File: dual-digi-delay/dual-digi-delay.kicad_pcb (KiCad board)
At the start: 2 copper layers, 148.8 x 152.9 mm, 214 parts, among them J1 TopBoardPowerRecv, J10 Delay Time Control, J11 Delay1_CV, J12 Delay1_CV, J13 Delay Send, J14 LowerBoardPowerSend, J15 Main Power, J16 Feedback Audio, J2 DelayAudio, J20 MidBoardPowerSend, J21 Delay Time Control, J23 Delay Out, J24 Output Audio, J25 DELAY2_CV, J26 DELAY1_CV, J27 AUDIO_IN, J28 MIX_OUT, J29 DELAY1_WET_OUT, J3 Input Audio, J30 DELAY2_WET_OUT, J31 Feedback Audio, J32 Delay Send, J33 Delay Return, J38 Delay2_CV, J39 Delay2_CV, J4 Output Audio, J5 Delay Out, J6 DelayAudio, J7 Input Audio, J8 Delay Return, J9 MidBoardPowerRecv, Q1 2N3904, Q2 2N3904, Q3 2N3904, Q4 2N3904, Q5 2N3904, Q6 2N3904, SW1 CV_JOIN, SW2 Delay 2 Input, U1 TL072, U2 TL072, U3 PT2399, U4 PT2399, U5 TL074, U6 TL074, U7 LM7805_TO220, U8 TL072

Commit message: Finalising rev 01 of dual digi delay
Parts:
- added G***: LOGO, rumblesan-footprints:Logo_Ammonite-simple_10.4mmx12.0mm, B.Cu at (145.8, 34.8)
- R37, R43: value 100k -> 220k
- R42: value 47k -> 100k
- moved R44 28.6 mm to (110.5, 107.7)
- moved R39 27.5 mm to (92.2, 134.6)
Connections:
- net /Power/+V renamed +12V
- net /Power/-V renamed -12V
- H1 pad 1: /TOP_0V -> GND
- H2 pad 1: /TOP_0V -> GND
- H3 pad 1: /MID_0V -> GND
- H4 pad 1: /MID_0V -> GND
- R39 pad 2: /MID_+V -> /MID_-V
- R44 pad 2: /MID_+V -> /MID_-V
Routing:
- net Net-(C44-Pad2): track 41.7 -> 29.4 mm
- net Net-(C43-Pad2): track 30.0 -> 42.1 mm
- net /MID_-V: track 179.7 -> 186.0 mm
- net /MID_+V: track 155.6 -> 149.7 mm
- net Net-(C41-Pad1): track 28.6 -> 30.2 mm
- net /CVControl/DELAY1_CV_JOIN_OUT: track 38.9 -> 39.7 mm
- net /MID_0V: vias 20 -> 26

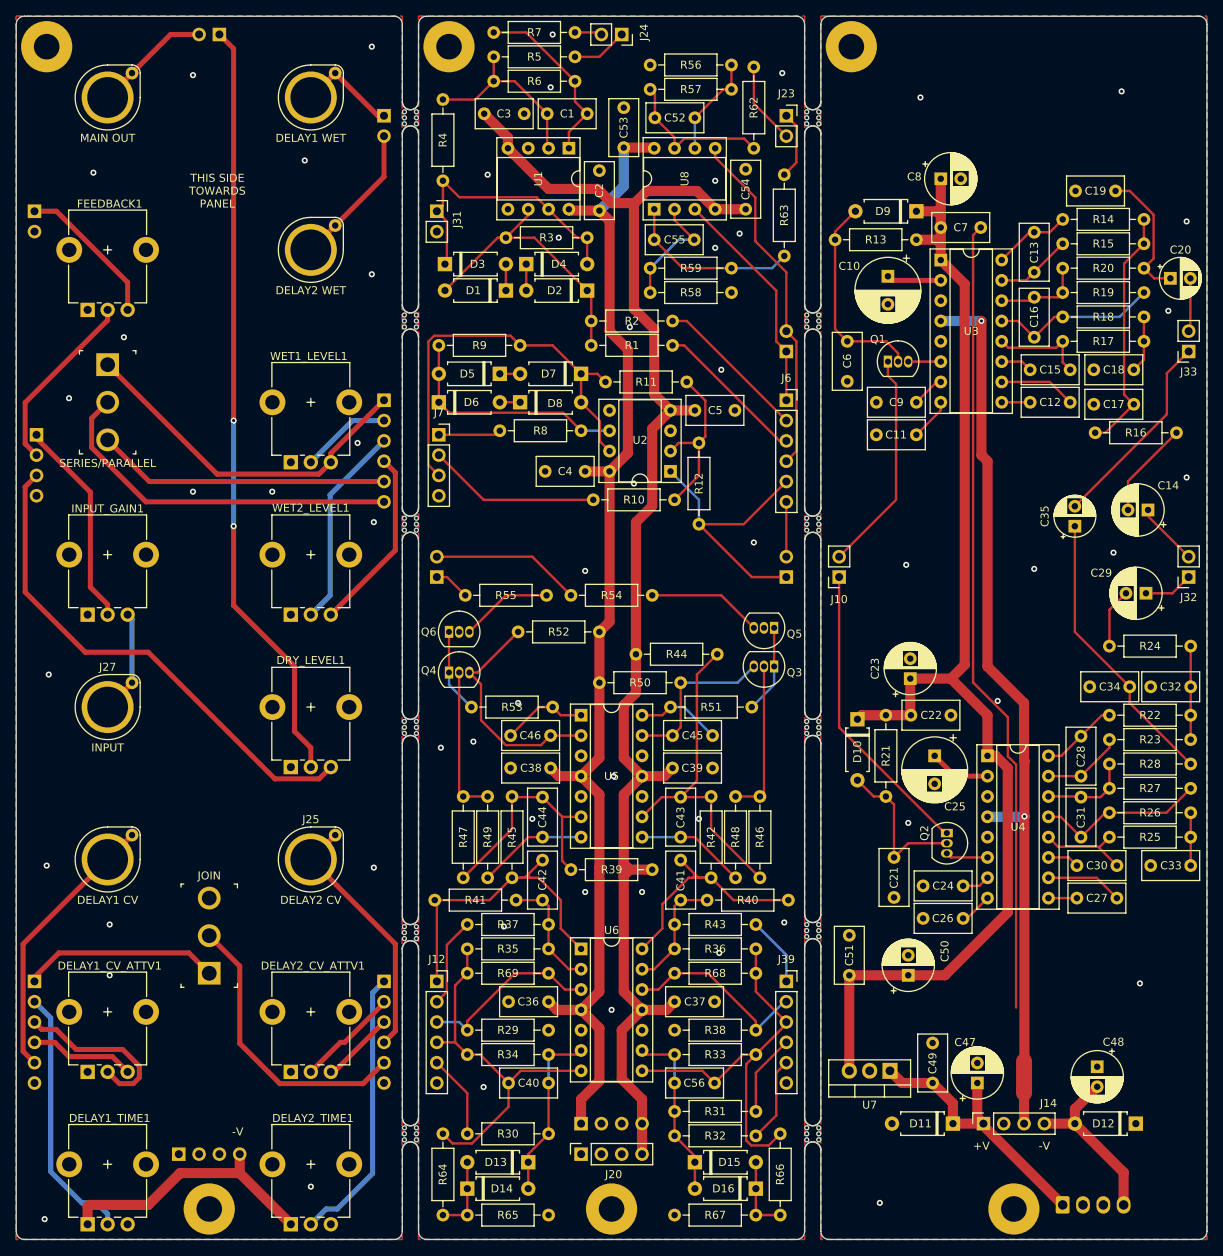
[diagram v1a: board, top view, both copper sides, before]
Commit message: Updating digi delay to rev 2
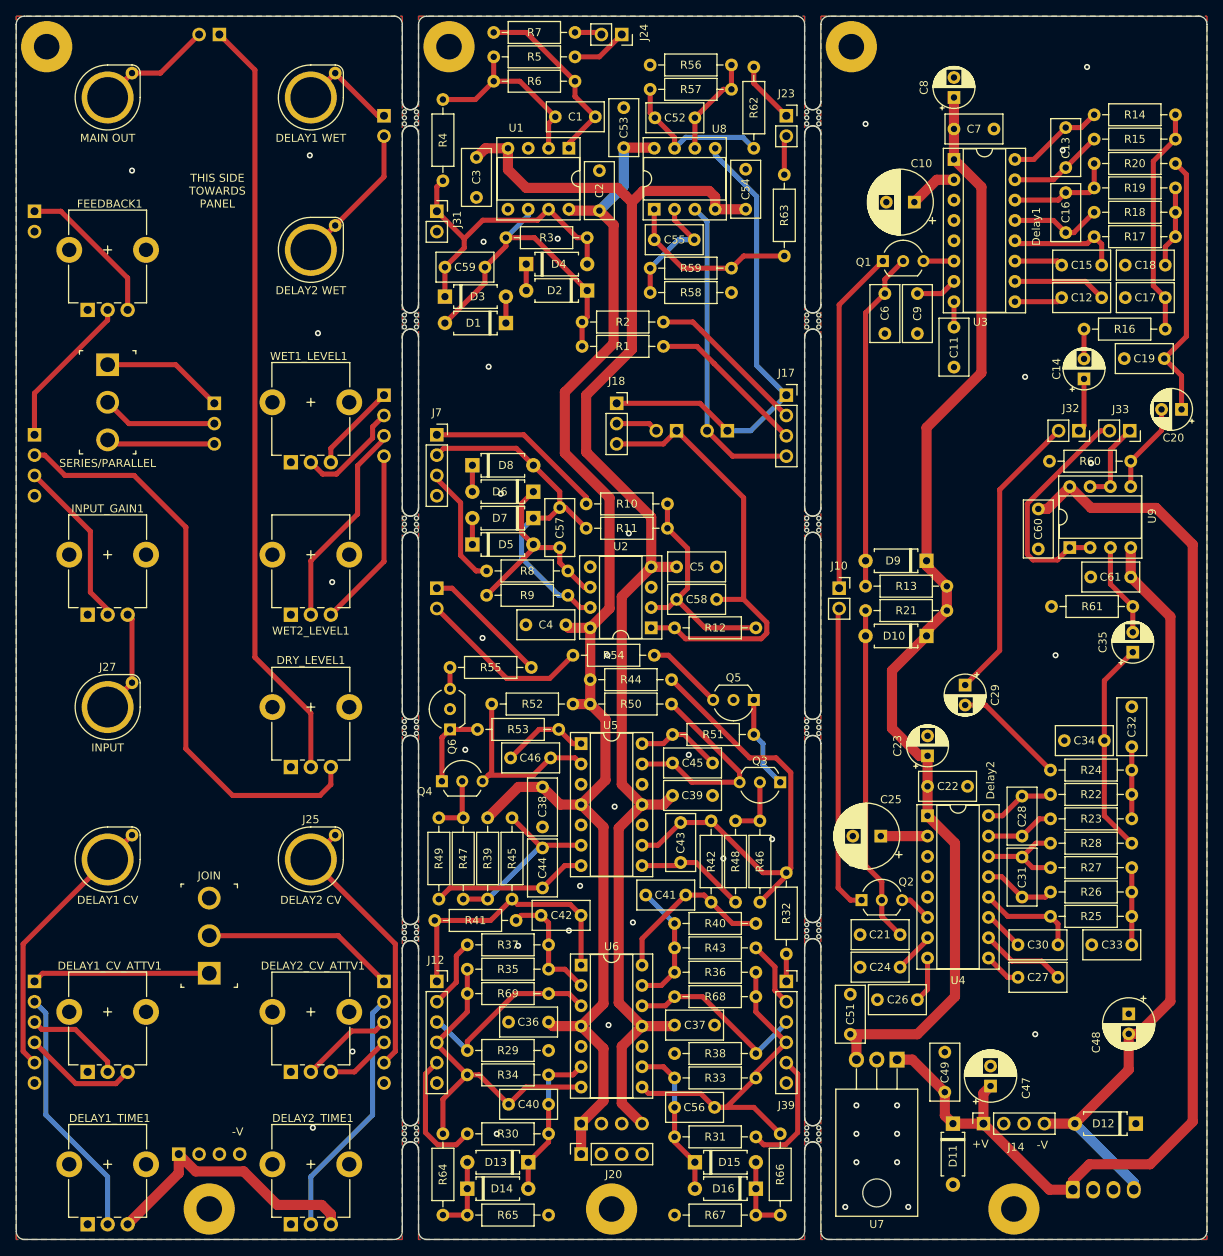
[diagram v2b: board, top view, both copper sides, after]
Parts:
- removed C50: 10uF, rumblesan-footprints:CP_Radial_D6.3mm_P2.50mm
- removed G***: LOGO, rumblesan-footprints:Logo_Ammonite-simple_10.4mmx12.0mm
- removed NT1: Net-Tie_2, NetTie:NetTie-2_SMD_Pad2.0mm
- removed mouse-bite-2mm-slot (x12): VAL**, Panelization:mouse-bite-2mm-slot
- added C57: 10pF, rumblesan-footprints:C_Rect_L7.0mm_W3.5mm_P5.00mm, F.Cu at (90.8, 89.4)
- added C58: 10pF, rumblesan-footprints:C_Rect_L7.0mm_W3.5mm_P5.00mm, F.Cu at (110.4, 100.8)
- added C59: 10pF, rumblesan-footprints:C_Rect_L7.0mm_W3.5mm_P5.00mm, F.Cu at (76.5, 59.3)
- added C60: 100nF, rumblesan-footprints:C_Rect_L7.0mm_W3.5mm_P5.00mm, F.Cu at (150.6, 94.5)
- added C61: 100nF, rumblesan-footprints:C_Rect_L7.0mm_W3.5mm_P5.00mm, F.Cu at (162.2, 98.0)
- added H10: MouseBite, Panelization:mouse-bite-2mm-slot, F.Cu at (72.1, 142.5)
- added H11: MouseBite, Panelization:mouse-bite-2mm-slot, F.Cu at (72.1, 91.4)
- added H12: MouseBite, Panelization:mouse-bite-2mm-slot, F.Cu at (122.4, 40.6)
- added H13: MouseBite, Panelization:mouse-bite-2mm-slot, F.Cu at (72.1, 40.6)
- added H14: MouseBite, Panelization:mouse-bite-2mm-slot, F.Cu at (72.1, 116.8)
- added H15: MouseBite, Panelization:mouse-bite-2mm-slot, F.Cu at (122.4, 167.6)
- added H16: MouseBite, Panelization:mouse-bite-2mm-slot, F.Cu at (122.4, 66.0)
- added H17: MouseBite, Panelization:mouse-bite-2mm-slot, F.Cu at (72.1, 66.0)
- added H18: MouseBite, Panelization:mouse-bite-2mm-slot, F.Cu at (122.4, 142.2)
- added H19: Logo_Ammonite-simple, rumblesan-footprints:Logo_Ammonite-simple_10.4mmx12.0mm, B.Cu at (134.1, 82.7)
- added H7: MouseBite, Panelization:mouse-bite-2mm-slot, F.Cu at (72.1, 167.6)
- added H8: MouseBite, Panelization:mouse-bite-2mm-slot, F.Cu at (122.4, 91.4)
- added H9: MouseBite, Panelization:mouse-bite-2mm-slot, F.Cu at (122.4, 116.8)
- added J17: Delay Audio, Connector_PinSocket_2.54mm:PinSocket_1x04_P2.54mm_Vertical, F.Cu at (119.1, 75.3)
- added J18: Delay2 Source, Connector_PinSocket_2.54mm:PinSocket_1x03_P2.54mm_Vertical, F.Cu at (97.9, 76.3)
- added R60: 100k, rumblesan-footprints:Resistor_THT_L6.3mm_D2.5mm_P10.16mm_Horizontal, F.Cu at (162.2, 83.6)
- added R61: 100k, rumblesan-footprints:Resistor_THT_L6.3mm_D2.5mm_P10.16mm_Horizontal, F.Cu at (162.4, 101.7)
- added U9: TL072, rumblesan-footprints:DIP-8_W7.62mm_Socket, F.Cu at (154.6, 94.4)
- C13, C28: value 100nF -> 560pF
- C14, C29: value 4.7uF -> 10uF; footprint rumblesan-footprints:CP_Radial_D6.3mm_P2.50mm -> rumblesan-footprints:CP_Radial_D5.0mm_P2.50mm
- C20, C35: value 1uF -> 10uF
- C23, C8: footprint rumblesan-footprints:CP_Radial_D6.3mm_P2.50mm -> rumblesan-footprints:CP_Radial_D5.0mm_P2.50mm
- J2: value DelayAudio -> Delay Audio; footprint Connector_PinHeader_2.54mm:PinHeader_1x06_P2.54mm_Vertical -> Connector_PinHeader_2.54mm:PinHeader_1x04_P2.54mm_Vertical
- J25: value DELAY2_CV -> BananaJack_PanelMount
- J26: value DELAY1_CV -> BananaJack_PanelMount
- J27: value AUDIO_IN -> BananaJack_PanelMount
- J28: value MIX_OUT -> BananaJack_PanelMount
- J29: value DELAY1_WET_OUT -> BananaJack_PanelMount
- J30: value DELAY2_WET_OUT -> BananaJack_PanelMount
- J6: value DelayAudio -> Delay2 Source; footprint Connector_PinSocket_2.54mm:PinSocket_1x06_P2.54mm_Vertical -> Connector_PinHeader_2.54mm:PinHeader_1x03_P2.54mm_Vertical; moved to B.Cu
- Q1, Q2, Q3, Q4, Q5, Q6: footprint Package_TO_SOT_THT:TO-92_Inline -> Package_TO_SOT_THT:TO-92_Inline_Wide
- R1, R2: value 100k -> 47k
- R13, R21: value 220k -> 560k
- R32, R42, R45: value 100k -> 56k
- R39, R44: value 220k -> 150k
- R4, R5, R56, R58: value 27k -> 15k
- R57, R59: value 82k -> 100k
- R9: value 27k -> 33k
- SW1: value CV_JOIN -> SW_SPST
- SW2: value Delay 2 Input -> SW_SPDT
- U7: footprint Package_TO_SOT_THT:TO-220-3_Vertical -> Package_TO_SOT_THT:TO-220-3_Horizontal_TabDown
- moved J6 71.5 mm to (47.6, 76.3), turned to 180 degrees
- moved D9 43.7 mm to (136.7, 96.0)
- moved R13 43.5 mm to (139.2, 99.2)
- moved R9 31.8 mm to (91.8, 100.3)
- moved C29 25.3 mm to (141.5, 111.5), turned to 270 degrees
- moved R32 23.1 mm to (119.1, 145.2), turned to 90 degrees
- moved J13 22.9 mm to (105.4, 79.8), turned to 90 degrees
- moved J32 22.9 mm to (155.7, 79.8), turned to 270 degrees
- moved C19 21.8 mm to (161.4, 70.7)
- moved D5 21.6 mm to (79.9, 94.0), turned to 0 degrees
- moved U2 19.7 mm to (102.2, 104.4)
- moved C5 19.7 mm to (105.4, 96.8)
- moved C4 19.3 mm to (86.6, 104.0)
- moved D7 19.0 mm to (87.5, 90.7)
- moved R11 18.4 mm to (104.3, 91.9)
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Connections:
- C14 pad 1: /PT2399-Delay-2/AUDIO_IN -> /PT2399-Delay-1/AUDIO_IN
- C2 pad 1: /MID_0V -> GND
- C2 pad 2: /MID_+V -> +12V
- C20 pad 2: /PT2399-Delay-2/AUDIO_OUT -> /PT2399-Delay-1/AUDIO_OUT
- C29 pad 1: /PT2399-Delay-1/AUDIO_IN -> /PT2399-Delay-2/AUDIO_IN
- C3 pad 1: /MID_-V -> -12V
- C3 pad 2: /MID_0V -> GND
- C35 pad 2: /PT2399-Delay-1/AUDIO_OUT -> /PT2399-Delay-2/AUDIO_OUT
- C36 pad 1: /MID_0V -> GND
- C36 pad 2: /MID_+V -> +12V
- C37 pad 1: /MID_-V -> -12V
- C37 pad 2: /MID_0V -> GND
- C38 pad 1: /MID_0V -> GND
- C38 pad 2: /MID_+V -> +12V
- C39 pad 1: /MID_-V -> -12V
- C39 pad 2: /MID_0V -> GND
- C4 pad 1: /MID_0V -> GND
- C4 pad 2: /MID_+V -> +12V
- C5 pad 1: /MID_-V -> -12V
- C5 pad 2: /MID_0V -> GND
- C53 pad 1: /MID_0V -> GND
- C53 pad 2: /MID_+V -> +12V
- C54 pad 1: /MID_-V -> -12V
- C54 pad 2: /MID_0V -> GND
- DELAY1_CV_ATTV1 pad 1: /TOP_0V -> GND
- DELAY1_TIME1 pad 1: /CVInputs/-V -> GND
- DELAY1_TIME1 pad 3: /TOP_0V -> +12V
- DELAY2_CV_ATTV1 pad 1: /TOP_0V -> GND
- DELAY2_TIME1 pad 1: /CVInputs/-V -> GND
- DELAY2_TIME1 pad 3: /TOP_0V -> +12V
- DRY_LEVEL1 pad 1: /TOP_0V -> GND
- FEEDBACK1 pad 1: /TOP_0V -> GND
- INPUT_GAIN1 pad 1: /TOP_0V -> GND
- J1 pad 1: /TOP_0V -> +12V
- J1 pad 2: /TOP_0V -> GND
- J1 pad 3: /TOP_0V -> GND
- J1 pad 4: /CVInputs/-V -> GND
- J11 pad 6: /TOP_0V -> GND
- J12 pad 6: /MID_0V -> GND
- J16 pad 2: /TOP_0V -> GND
- J20 pad 1: /MID_0V -> +12V
- J20 pad 2: /MID_0V -> GND
- J20 pad 3: /MID_0V -> GND
- J20 pad 4: /MID_-V -> GND
- J3 pad 1: /AudioIO/AUDIO_IN -> /AudioIO/FEEDBACK_LEVEL
- J3 pad 2: /AudioIO/FEEDBACK_LEVEL -> /AudioIO/DRY_AUDIO_INPUT
- J3 pad 3: /AudioIO/DRY_AUDIO_INPUT -> /AudioIO/AUDIO_IN
- J3 pad 4: /TOP_0V -> GND
- J31 pad 2: /MID_0V -> GND
- J33 pad 1: /PT2399-Delay-1/AUDIO_OUT -> /DelayBuffers/DELAY1_OUT
- J33 pad 2: /PT2399-Delay-2/AUDIO_OUT -> /DelayBuffers/DELAY2_OUT
- J38 pad 1: /CVInputs/DELAY2_CONTROL -> /CVInputs/JOIN_CV
- J38 pad 2: /CVInputs/DELAY2_CV_ATTV -> /CVInputs/DELAY2_CONTROL
- J38 pad 3: /CVInputs/DELAY2_CV_CTRL -> /CVInputs/DELAY2_CV_ATTV
- J38 pad 4: /CVInputs/DELAY2_CV_INPUT -> /CVInputs/DELAY2_CV_CTRL
- J38 pad 5: /CVInputs/JOIN_CV -> /CVInputs/DELAY2_CV_INPUT
- J38 pad 6: /TOP_0V -> GND
- J39 pad 1: /CVControl/DELAY2_CONTROL -> /CVControl/DELAY2_JOIN_CV_INPUT
- J39 pad 2: /CVControl/DELAY2_CV_ATTV -> /CVControl/DELAY2_CONTROL
- J39 pad 3: /CVControl/DELAY2_CV_CTRL -> /CVControl/DELAY2_CV_ATTV
- J39 pad 4: /CVControl/DELAY2_CV_INPUT1 -> /CVControl/DELAY2_CV_CTRL
- J39 pad 5: /CVControl/DELAY2_CV_INPUT2 -> /CVControl/DELAY2_CV_INPUT
- J39 pad 6: /MID_0V -> GND
- J6 pad 1: /DelayOut/DELAY1_WET -> /AudioIO/DELAY1_WET_TO_2
- J6 pad 2: /OutputMix/DELAY1_WET_LEVEL -> /AudioIO/DELAY2_SOURCE
- J6 pad 3: /OutputMix/DELAY2_WET_LEVEL -> /AudioIO/INPUT_MIX
- J7 pad 1: /InputMix/AUDIO_IN -> /InputMix/DELAY_FEEDBACK
- J7 pad 2: /InputMix/DELAY_FEEDBACK -> /InputMix/DRY_AUDIO_SOURCE
- J7 pad 3: /InputMix/DRY_AUDIO_SOURCE -> /InputMix/AUDIO_IN
- J7 pad 4: /MID_0V -> GND
- J9 pad 1: /MID_+V -> +12V
- J9 pad 2: /MID_0V -> GND
- J9 pad 3: /MID_0V -> GND
- J9 pad 4: /MID_-V -> -12V
- Q1 pad 1: /PT2399-Delay-2/DELAY_TIME_CTRL -> /PT2399-Delay-1/DELAY_TIME_CTRL
- Q2 pad 1: /PT2399-Delay-1/DELAY_TIME_CTRL -> /PT2399-Delay-2/DELAY_TIME_CTRL
- Q5 pad 2: /MID_0V -> GND
- Q6 pad 2: /MID_0V -> GND
- R19 pad 1: Net-(C16-Pad2) -> Net-(C18-Pad2)
- R27 pad 1: Net-(C31-Pad2) -> Net-(C33-Pad2)
- R29 pad 1: /MID_0V -> GND
- R31 pad 1: /CVControl/DELAY2_CV_INPUT1 -> /CVControl/DELAY2_CV_INPUT
- R32 pad 1: /CVControl/DELAY2_CV_INPUT2 -> /CVControl/DELAY2_JOIN_CV_INPUT
- R32 pad 2: Net-(C56-Pad2) -> Net-(C43-Pad2)
- R38 pad 1: /MID_0V -> GND
- R39 pad 2: /MID_-V -> +12V
- R44 pad 2: /MID_-V -> +12V
- R50 pad 1: /MID_+V -> +12V
- R52 pad 1: /MID_+V -> +12V
- R56 pad 1: /MID_0V -> GND
- R58 pad 1: /MID_0V -> GND
- R62 pad 1: /DelayOut/DELAY2_WET_OUT -> /DelayOut/DELAY1_WET_OUT
- R63 pad 1: /DelayOut/DELAY1_WET_OUT -> /DelayOut/DELAY2_WET_OUT
- R65 pad 1: /MID_0V -> GND
- R67 pad 1: /MID_0V -> GND
- SW2 pad 1: /AudioIO/DELAY1_WET -> /AudioIO/DELAY1_WET_TO_2
- U1 pad 3: /MID_0V -> GND
- U1 pad 4: /MID_-V -> -12V
- U1 pad 5: /MID_0V -> GND
- U1 pad 8: /MID_+V -> +12V
- U2 pad 3: /MID_0V -> GND
- U2 pad 4: /MID_-V -> -12V
- U2 pad 5: /MID_0V -> GND
- U2 pad 8: /MID_+V -> +12V
- U3 pad 4: GNDD -> GND
- U4 pad 4: GNDD -> GND
- U5 pad 10: /MID_0V -> GND
- U5 pad 11: /MID_-V -> -12V
- U5 pad 12: /MID_0V -> GND
- U5 pad 3: /MID_0V -> GND
- U5 pad 4: /MID_+V -> +12V
- U5 pad 5: /MID_0V -> GND
- U6 pad 10: /MID_0V -> GND
- U6 pad 11: /MID_-V -> -12V
- U6 pad 4: /MID_+V -> +12V
- U6 pad 5: /MID_0V -> GND
- U8 pad 3: /DelayOut/DELAY1_WET -> /DelayOut/DELAY2_WET
- U8 pad 4: /MID_-V -> -12V
- U8 pad 5: /DelayOut/DELAY2_WET -> /DelayOut/DELAY1_WET
- U8 pad 8: /MID_+V -> +12V
- WET1_LEVEL1 pad 1: /TOP_0V -> GND
- WET2_LEVEL1 pad 1: /TOP_0V -> GND
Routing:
- net +12V: track 35.6 -> 356.9 mm
- net -12V: track 22.3 -> 275.3 mm
- net /MID_-V: track 186.0 -> 0.00 mm
- net /MID_+V: track 149.7 -> 0.00 mm
- net GNDD: track 104.5 -> 0.00 mm, vias 2 -> 0
- net GND: track 103.9 -> 0.00 mm, vias 12 -> 40
- net /CVInputs/-V: track 34.5 -> 0.00 mm
- net /AudioIO/DELAY1_WET: track 44.7 -> 11.1 mm
- net /AudioIO/DELAY2_SOURCE: track 45.8 -> 14.4 mm
- net /DelayOut/DELAY1_WET: track 28.6 -> 59.0 mm
- net /DelayBuffers/DELAY2_OUT: track 0.00 -> 29.1 mm
- net /PT2399-Delay-2/AUDIO_IN: track 7.95 -> 36.6 mm
- net /AudioIO/INPUT_MIX: track 36.7 -> 13.5 mm
- net Net-(C21-Pad1): track 19.8 -> 42.3 mm
- net /InputMix/INPUT_MIX: track 34.9 -> 56.8 mm
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- removed copper zone on B.Cu, net /MID_0V
- removed copper zone on F.Cu, net /MID_0V
- removed copper zone on B.Cu, net /TOP_0V
- removed copper zone on F.Cu, net /TOP_0V
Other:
- board text added: "Delay1"
- board text added: "Delay2"
- board text added: "Dual PT2399 Digi Delay Revision 02"
- board text removed: "Dual PT2399 Digi Delay Revision 01"
